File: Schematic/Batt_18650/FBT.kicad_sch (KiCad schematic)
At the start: 19 parts, among them J1 TRRS Connector 3.5, J2 TRRS Connector 3.5, SW1 SW_SPDT, U1 HT7333-1-TO92

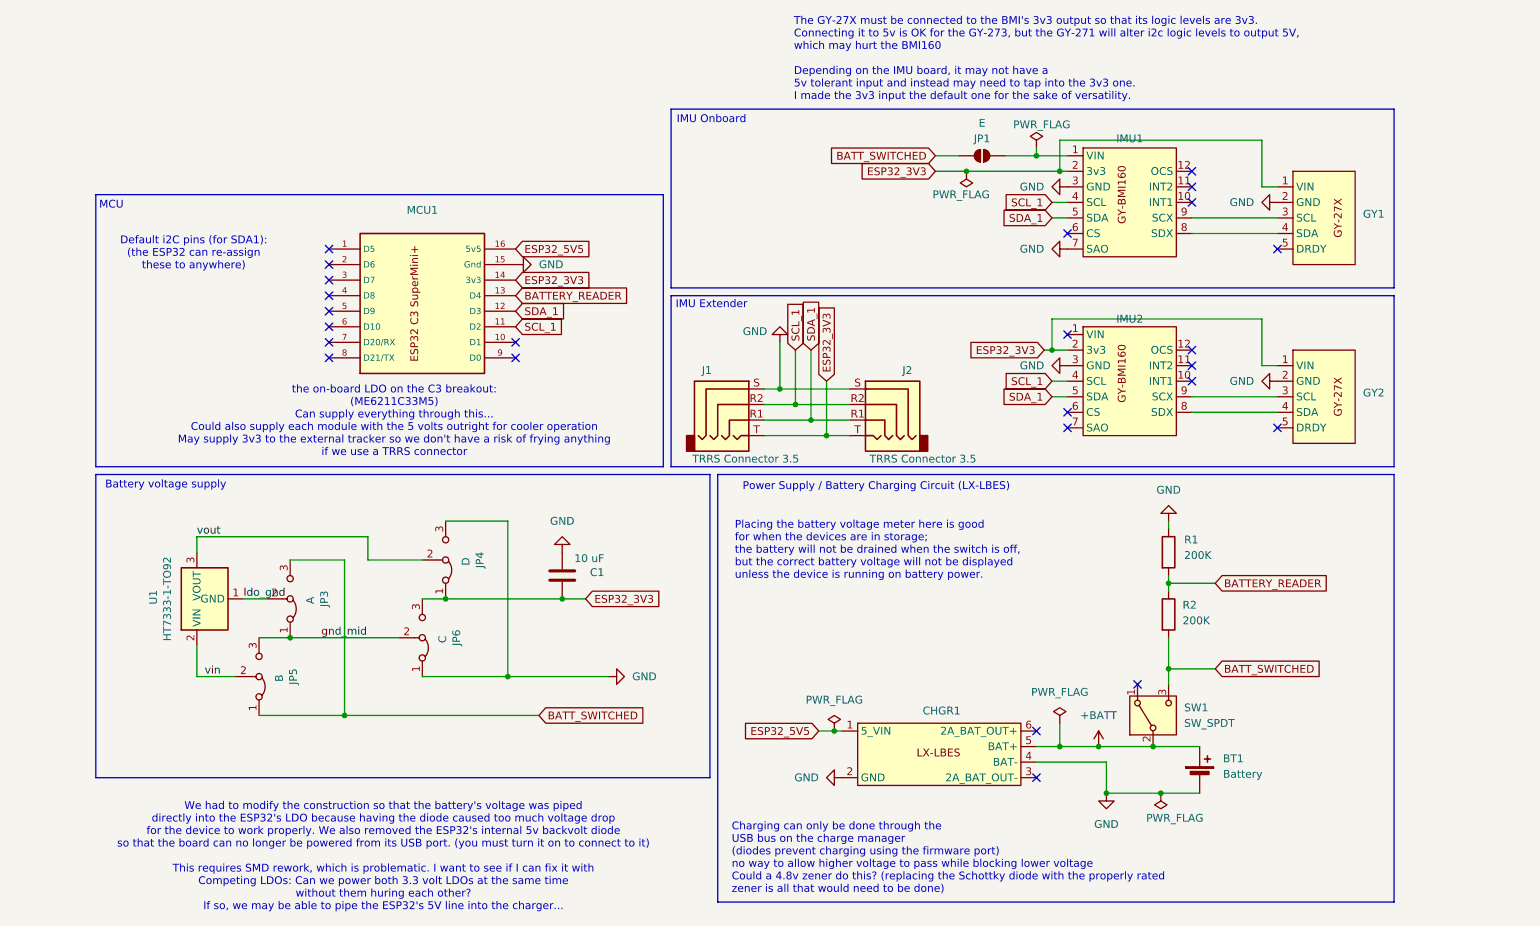
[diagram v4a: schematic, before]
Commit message: Slight PCB tweaking
Double-checking that everything is correct before I ship off the next batch for fabbing.
Added a jumper pad between usb-c 5v inputs.
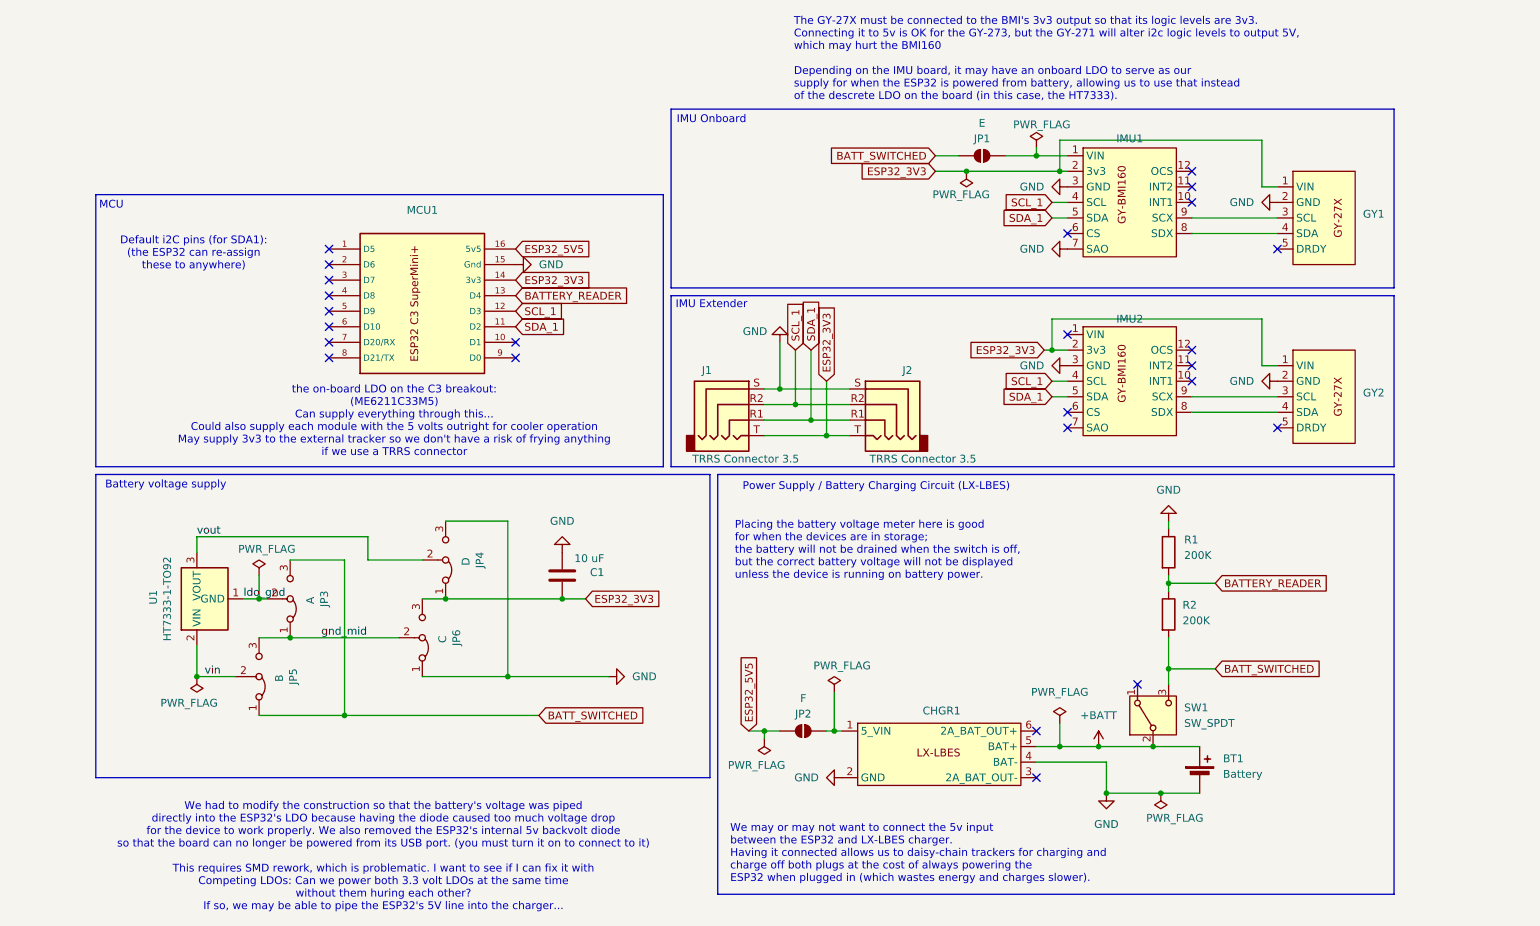
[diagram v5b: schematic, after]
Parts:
- added JP2: F, Jumper:SolderJumper-2_P1.3mm_Open_RoundedPad1.0x1.5mm, symbol Jumper:SolderJumper_2_Open
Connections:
- net ESP32_5V5: now also JP2.2 (B); no longer CHGR1.1 (5_VIN)
- net SCL_1: now also MCU1.12 (D3); no longer MCU1.11 (D2)
- net SDA_1: now also MCU1.11 (D2); no longer MCU1.12 (D3)
- new net: CHGR1.1 (5_VIN), JP2.1 (A)
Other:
- note added: "The GY-27X must be connected to the BMI's 3v3 output so that its logic levels are 3v3. Connecting it to 5v is OK for the GY-273, but the GY-271 will alter i2c logic levels to output 5V, which may hurt the BMI160 Depending on the IMU board, it may have an onboard LDO to serve as our supply for when the ESP32 is powered from battery, allowing us to use that instead of the descrete LDO on the board 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"
- note added: "We may or may not want to connect the 5v input between the ESP32 and LX-LBES charger. Having it connected allows us to daisy-chain trackers for charging and charge off both plugs at the cost of always powering the ESP32 when plugged in (which wastes energy and charges slower)."
- note removed: "Charging can only be done through the USB bus on the charge manager (diodes prevent charging using the firmware port) no way to allow higher voltage to pass while blocking lower voltage Could a 4.8v zener do this? (replacing the Schottky diode with the properly rated zener is all that would need to be done)"
- note removed: "The GY-27X must be connected to the BMI's 3v3 output so that its logic levels are 3v3. Connecting it to 5v is OK for the GY-273, but the GY-271 will alter i2c logic levels to output 5V, which may hurt the BMI160 Depending on the IMU board, it may not have a 5v tolerant input and instead may need to tap into the 3v3 one. I made the 3v3 input the default one for the sake of versatility."
